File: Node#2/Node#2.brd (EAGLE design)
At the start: 100 x 80 mm, 75 parts, among them IC1 TSL25911FN, J1 68712414522, Q2 SI1308EDL-T1-GE3, U2 RV8564C3, U4 TPS63001DRCT

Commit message: Node#2 sorted, Node#1 small adjusts
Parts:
- added R2: 100, rcl:R0805
- added U$9: BZB984, BlueHome:SOT95P230X110-3N
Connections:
- new net N$2: D2.A, R2.1
- net +3V3: no longer D2.A
- net +3V3_RTC: now also U$9.2
- net GND: now also U$9.3
- net V+: now also R2.2

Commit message: Schematic finished (hopefully) !
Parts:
- added C34: (no value), rcl:C0805
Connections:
- removed net N$26: C31.2, C33.2, MK1.5
- net +3V3: now also MK1.5
- net +5V: no longer U$1.2
- net ADC2: now also C34.1
- net GND: now also C31.2, C33.2, C34.2
- net V+: now also U$1.2
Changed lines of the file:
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@@
 <layers>
 <layer number="1" name="Top" color="4" fill="1" visible="yes" active="yes"/>
+<layer number="2" name="Route2" color="1" fill="3" visible="no" active="no"/>
+<layer number="3" name="Route3" color="4" fill="3" visible="no" active="no"/>
+<layer number="4" name="Route4" color="1" fill="4" visible="no" active="no"/>
+<layer number="5" name="Route5" color="4" fill="4" visible="no" active="no"/>
+<layer number="6" name="Route6" color="1" fill="8" visible="no" active="no"/>
+<layer number="7" name="Route7" color="4" fill="8" visible="no" active="no"/>
+<layer number="8" name="Route8" color="1" fill="2" visible="no" active="no"/>
+<layer number="9" name="Route9" color="4" fill="2" visible="no" active="no"/>
+<layer number="10" name="Route10" color="1" fill="7" visible="no" active="no"/>
+<layer number="11" name="Route11" color="4" fill="7" visible="no" active="no"/>
+<layer number="12" name="Route12" color="1" fill="5" visible="no" active="no"/>
+<layer number="13" name="Route13" color="4" fill="5" visible="no" active="no"/>
+<layer number="14" name="Route14" color="1" fill="6" visible="no" active="no"/>
+<layer number="15" name="Route15" color="4" fill="6" visible="no" active="no"/>
 <layer number="16" name="Bottom" color="1" fill="1" visible="yes" active="yes"/>
 <layer number="17" name="Pads" color="2" fill="1" visible="yes" active="yes"/>
@@
 <attribute name="VALUE" x="-66.573359375" y="-773.99578125" size="1.27236875" layer="27"/>
 </element>
+<element name="C34" library="rcl" package="C0805" value="" x="-64.77" y="-778.51" smashed="yes">
+<attribute name="NAME" x="-66.04" y="-777.24" size="1.27" layer="25"/>
+<attribute name="VALUE" x="-66.04" y="-781.05" size="1.27" layer="27"/>
+</element>
 </elements>
 <signals>
@@
 <contactref element="C8" pad="1"/>
 <contactref element="U$9" pad="3"/>
+<contactref element="C34" pad="2"/>
+<contactref element="C33" pad="2"/>
+<contactref element="C31" pad="2"/>
 <wire x1="-55.56" y1="-447.04" x2="-55.56" y2="-453.39" width="0" layer="19" extent="1-1"/>
 <wire x1="-55.56" y1="-440.69" x2="-55.56" y2="-447.04" width="0" layer="19" extent="1-1"/>
 <wire x1="-55.56" y1="-434.34" x2="-55.56" y2="-440.69" width="0" layer="19" extent="1-1"/>
 <wire x1="-55.56" y1="-427.99" x2="-55.56" y2="-434.34" width="0" layer="19" extent="1-1"/>
-<wire x1="-55.56" y1="-478.79" x2="-55.56" y2="-453.39" width="0" layer="19" extent="1-1"/>
+<wire x1="-53.66" y1="-459.74" x2="-55.56" y2="-453.39" width="0" layer="19" extent="1-1"/>
+<wire x1="-53.66" y1="-472.44" x2="-53.66" y2="-459.74" width="0" layer="19" extent="1-1"/>
+<wire x1="-55.56" y1="-478.79" x2="-53.66" y2="-472.44" width="0" layer="19" extent="1-1"/>
 <wire x1="-58.9" y1="-499.11" x2="-55.56" y2="-478.79" width="0" layer="19" extent="1-1"/>
 <wire x1="-53.66" y1="-381" x2="-55.56" y2="-427.99" width="0" layer="19" extent="1-1"/>
@@
 <wire x1="-59.69" y1="-756.92" x2="-63.82" y2="-734.06" width="0" layer="19" extent="1-1"/>
 <wire x1="-63.79" y1="-770.89" x2="-59.69" y2="-756.92" width="0" layer="19" extent="1-1"/>
+<wire x1="-63.82" y1="-778.51" x2="-63.79" y2="-770.89" width="0" layer="19" extent="1-1"/>
 </signal>
 <signal name="N$10">
@@
 <contactref element="C17" pad="1"/>
 <contactref element="C16" pad="1"/>
-<contactref element="C31" pad="1"/>
-<contactref element="C33" pad="1"/>
 <contactref element="L2" pad="1"/>
 <contactref element="C24" pad="1"/>
@@
 <contactref element="R3" pad="2"/>
 <contactref element="R8" pad="2"/>
+<contactref element="C31" pad="1"/>
+<contactref element="C33" pad="1"/>
+<contactref element="MK1" pad="5"/>
 <wire x1="-63.82" y1="-689.61" x2="-63.82" y2="-695.96" width="0" layer="19" extent="1-1"/>
 <wire x1="-63.82" y1="-702.31" x2="-63.82" y2="-695.96" width="0" layer="19" extent="1-1"/>
@@
 <wire x1="-55.56" y1="-252.73" x2="-55.56" y2="-259.08" width="0" layer="19" extent="1-1"/>
 <wire x1="-49.35" y1="-247.65" x2="-55.56" y2="-252.73" width="0" layer="19" extent="1-1"/>
-<wire x1="-40.32" y1="-148.59" x2="-49.35" y2="-247.65" width="0" layer="19" extent="1-1"/>
+<wire x1="-52.5025" y1="-241.209" x2="-49.35" y2="-247.65" width="0" layer="19" extent="1-1"/>
+<wire x1="-40.32" y1="-148.59" x2="-52.5025" y2="-241.209" width="0" layer="19" extent="1-1"/>
 <wire x1="-40.32" y1="-142.24" x2="-40.32" y2="-148.59" width="0" layer="19" extent="1-1"/>
 <wire x1="-40.32" y1="-88.9" x2="-40.32" y2="-142.24" width="0" layer="19" extent="1-1"/>
@@
 </signal>
 <signal name="+5V">
-<contactref element="U$1" pad="2"/>
 <contactref element="R5" pad="2"/>
-<wire x1="-44.54" y1="-240.03" x2="-63.82" y2="-676.91" width="0" layer="19" extent="1-1"/>
 </signal>
 <signal name="N$9">
@@
 <wire x1="-52.29" y1="-483.87" x2="-55.56" y2="-396.24" width="0" layer="19" extent="1-1"/>
 <wire x1="-55.4" y1="-502.92" x2="-52.29" y2="-483.87" width="0" layer="19" extent="1-1"/>
-</signal>
-<signal name="N$26">
-<contactref element="MK1" pad="5"/>
-<contactref element="C31" pad="2"/>
-<contactref element="C33" pad="2"/>
-<wire x1="-53.66" y1="-459.74" x2="-52.5025" y2="-241.209" width="0" layer="19" extent="1-1"/>
-<wire x1="-53.66" y1="-472.44" x2="-53.66" y2="-459.74" width="0" layer="19" extent="1-1"/>
 </signal>
 <signal name="N$22">
@@
 <contactref element="R5" pad="1"/>
 <contactref element="R17" pad="2"/>
+<contactref element="C34" pad="1"/>
 <wire x1="-65.72" y1="-676.91" x2="-63.82" y2="-683.26" width="0" layer="19" extent="1-1"/>
+<wire x1="-65.72" y1="-778.51" x2="-63.82" y2="-683.26" width="0" layer="19" extent="1-1"/>
 </signal>
 <signal name="V-">
@@
 <contactref element="C10" pad="1"/>
 <contactref element="R2" pad="2"/>
+<contactref element="U$1" pad="2"/>
 <wire x1="-38.42" y1="-154.94" x2="-40.32" y2="-161.29" width="0" layer="19" extent="1-1"/>
+<wire x1="-44.54" y1="-240.03" x2="-40.32" y2="-161.29" width="0" layer="19" extent="1-1"/>
 <wire x1="-37.0332" y1="-16.2306" x2="-38.42" y2="-154.94" width="0" layer="19" extent="1-1"/>
-<wire x1="-63.82" y1="-763.27" x2="-40.32" y2="-161.29" width="0" layer="19" extent="1-1"/>
+<wire x1="-63.82" y1="-763.27" x2="-44.54" y2="-240.03" width="0" layer="19" extent="1-1"/>
 </signal>
 <signal name="INT_HDC">

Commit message: Changed Packages, connected GPIO
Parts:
- added LS1: PS1720P02, BlueHome:PS17_1
- added Q1: BC847ALT1SMD, transistor-npn:SOT23
- added R11, R12, R13, R14, R19, R20, R21, R22, R23, R24, R25, R4, R6, R7: (no value), rcl:R0805
- L1: device rcl:L4532P -> rcl:L5038P
- L2: device rcl:L1812 -> rcl:L5038P
- moved U$8 53.4 mm to (0.00, -655.3)
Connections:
- net INT_HDC renamed DIO7
- net INT_RTC renamed DIO12
- net INT_SX renamed DIO13
- net INT_TSL renamed DIO6
- new net DIO0: J1.13
- new net DIO1: J1.12
- new net DIO2: J1.14
- new net DIO3: R4.1
- new net N$13: LED3.2, R19.2
- new net N$16: LED5.1, R22.2
- new net N$17: LED5.2, R23.2
- new net N$25: LED2.1, R12.2
- new net N$26: LED2.2, R13.2
- new net N$27: LED4.1, R21.2
- new net N$3: LS1.1, Q1.3, R6.1
- new net N$30: LED4.2, R20.2
- new net N$36: LED6.1, R24.2
- new net N$37: LED6.2, R25.2
- new net N$4: LED1.1, R7.2
- new net N$5: LED1.2, R11.2
- new net N$6: Q1.1, R4.2
- new net N$7: LED3.1, R14.2
- net +3V3: now also LS1.2, R6.2
- net CS: no longer J1.12
- net GND: now also Q1.2
- net LED0: now also R12.1, R14.1, R21.1, R22.1, R24.1, R7.1; no longer LED1.1, LED2.1, LED3.1, LED4.1, LED5.1, LED6.1
- net LED1: now also R11.1; no longer LED1.2
- net LED2: now also R13.1; no longer LED2.2
- net LED3: now also R19.1; no longer LED3.2
- net LED4: now also R20.1; no longer LED4.2
- net LED5: now also R23.1; no longer LED5.2
- net LED6: now also R25.1; no longer LED6.2
- net MOSI: no longer J1.14
- net SCLK: no longer J1.13

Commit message: Created node#2 Layout and Proximity Sensor in Library
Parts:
- U$7: value TOUCH_BUTTON -> PROXIMITY; device BlueHome:TOUCH_BUTTON -> BlueHome:PROXIMITY
- moved R24 958.0 mm to (30.2, 83.3), flipped to the bottom, turned to 270 degrees
- moved R22 948.1 mm to (27.7, 83.8), flipped to the bottom, turned to 270 degrees
- moved R21 942.8 mm to (25.1, 83.8), flipped to the bottom, turned to 270 degrees
- moved R23 936.1 mm to (37.2, 65.7)
- moved R25 934.9 mm to (64.4, 50.9)
- moved R14 925.9 mm to (22.6, 82.3), flipped to the bottom, turned to 270 degrees
- moved R20 924.0 mm to (37.5, 68.7)
- moved R19 921.3 mm to (35.7, 71.3)
- moved R6 919.7 mm to (33.5, 100.3), flipped to the bottom
- moved R13 912.6 mm to (28.7, 73.4), flipped to the bottom, turned to 180 degrees
- moved R12 912.0 mm to (22.6, 78.5), flipped to the bottom, turned to 180 degrees
- moved R4 905.7 mm to (56.1, 88.6), flipped to the bottom, turned to 90 degrees
- moved R11 905.1 mm to (27.2, 76.2), flipped to the bottom
- moved Q1 903.4 mm to (55.1, 94.2), flipped to the bottom
- moved LS1 900.3 mm to (45.7, 105.7), flipped to the bottom
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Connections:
- net N$33 renamed PROX_SENS
- removed net +5V: R5.2
- net V+: now also R5.2
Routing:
- net +3V3: track 0.00 -> 113.0 mm, vias 0 -> 2
- net N$1: track 0.00 -> 97.0 mm
- net VGL: track 0.00 -> 57.5 mm, vias 0 -> 2
- net +3V3_RTC: track 0.00 -> 54.9 mm, vias 0 -> 1
- net RESE: track 0.00 -> 53.4 mm, vias 0 -> 2
- net VGH: track 0.00 -> 51.8 mm, vias 0 -> 4
- net SDA: track 0.00 -> 44.0 mm, vias 0 -> 2
- net SCL: track 0.00 -> 38.7 mm, vias 0 -> 2
- net N$23: track 0.00 -> 37.0 mm, vias 0 -> 2
- net VSLR: track 0.00 -> 35.1 mm, vias 0 -> 2
- net V+: track 0.00 -> 34.0 mm
- net N$3: track 0.00 -> 31.9 mm, vias 0 -> 2
- net VSL: track 0.00 -> 30.8 mm, vias 0 -> 2
- net N$14: track 0.00 -> 28.5 mm, vias 0 -> 2
- net GDR: track 0.00 -> 26.0 mm
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- added copper zone on layer 1, net PROX_SENS
- removed copper zone on layer 1, net N$1
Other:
- board size 100 x 80 mm -> 60.5 x 120 mm

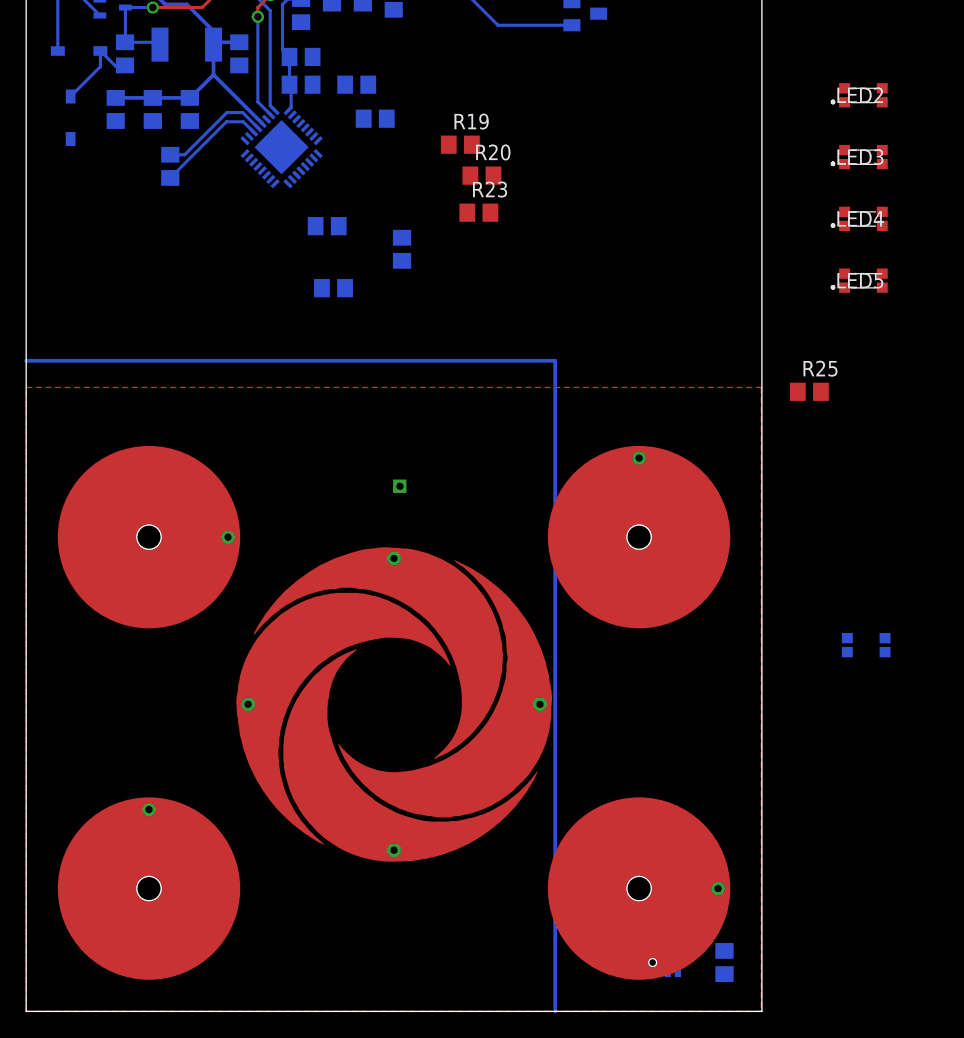
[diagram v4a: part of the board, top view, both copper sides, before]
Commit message: Worked on Layout on Node#2
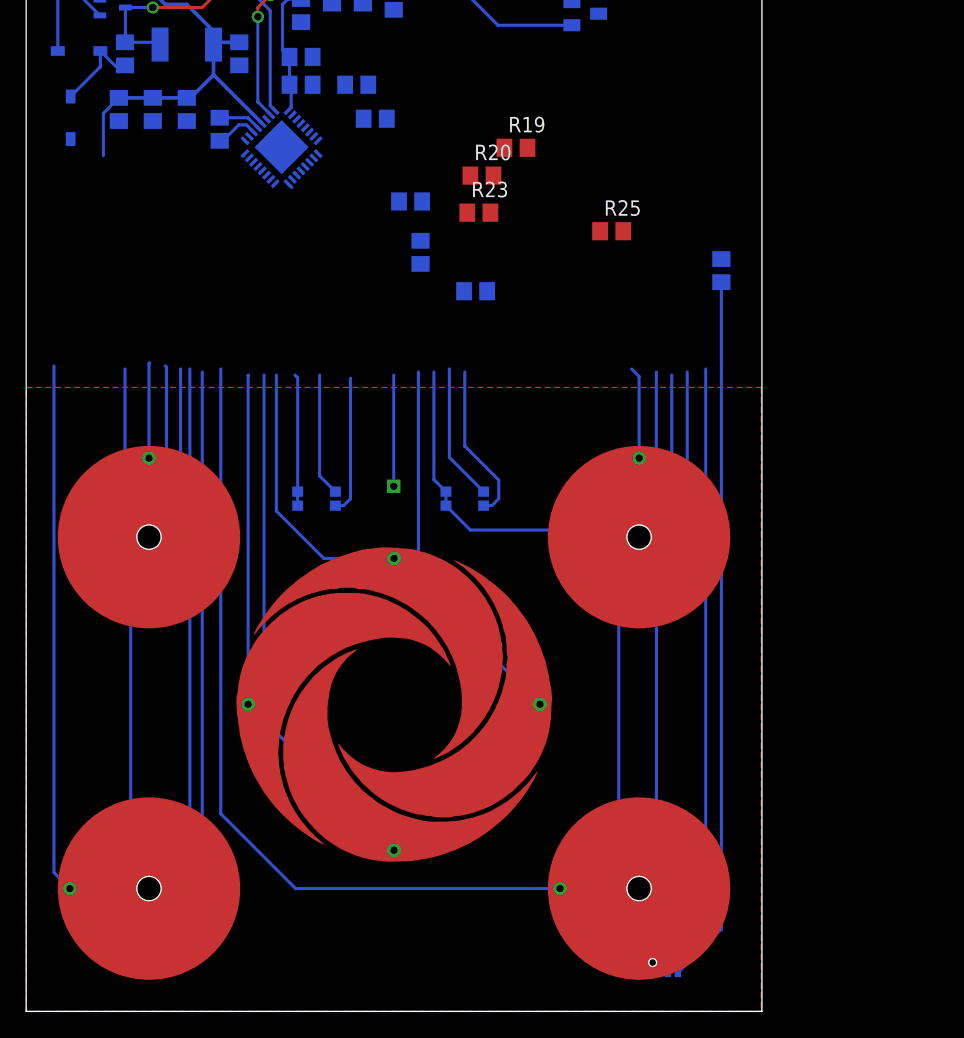
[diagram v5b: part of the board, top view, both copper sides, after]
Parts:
- moved LED3 84.1 mm to (10.1, 10.1), flipped to the bottom
- moved LED4 58.2 mm to (50.3, 10.1), flipped to the bottom
- moved C32 56.9 mm to (57.2, 60.9)
- moved U$4 49.6 mm to (50.4, 39.0)
- moved LED5 48.4 mm to (23.9, 42.2), flipped to the bottom
- moved LED2 40.7 mm to (50.5, 39.0), flipped to the bottom
- moved LED1 40.4 mm to (9.99, 39.0)
- moved U$3 40.3 mm to (10.1, 39.0)
- moved LED6 35.1 mm to (36.1, 42.2)
- moved U$5 28.9 mm to (10.1, 10.1), turned to 180 degrees
- moved R25 20.9 mm to (48.1, 64.2)
- moved C17 11.7 mm to (37.0, 59.2)
- moved C16 7.15 mm to (31.6, 66.6)
- moved C18 5.08 mm to (15.9, 72.5)
- moved R19 4.58 mm to (40.3, 71.0)
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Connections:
- removed net N$34: U$2.25
- net LED6: now also U$2.25
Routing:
- net +3V3: track 113.0 -> 236.5 mm
- net N$1: track 97.0 -> 0.00 mm
- net N$32: track 0.00 -> 67.0 mm
- net N$22: track 0.00 -> 58.3 mm
- net N$27: track 0.00 -> 45.8 mm
- net N$7: track 0.00 -> 44.7 mm
- net N$31: track 0.00 -> 43.5 mm
- net SEG3: track 0.00 -> 43.5 mm
- net N$30: track 0.00 -> 43.0 mm
- net N$13: track 0.00 -> 42.9 mm
- net SEG2: track 0.00 -> 31.5 mm
- net SEG4: track 0.00 -> 27.1 mm
- net SEG1: track 0.00 -> 22.5 mm
- net N$4: track 0.00 -> 15.3 mm
- net N$25: track 0.00 -> 14.6 mm
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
